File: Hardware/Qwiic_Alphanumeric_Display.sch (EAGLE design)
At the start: 16 parts, among them J1 PTH, J2 Qwiic Right Angle, U2 HT16K33

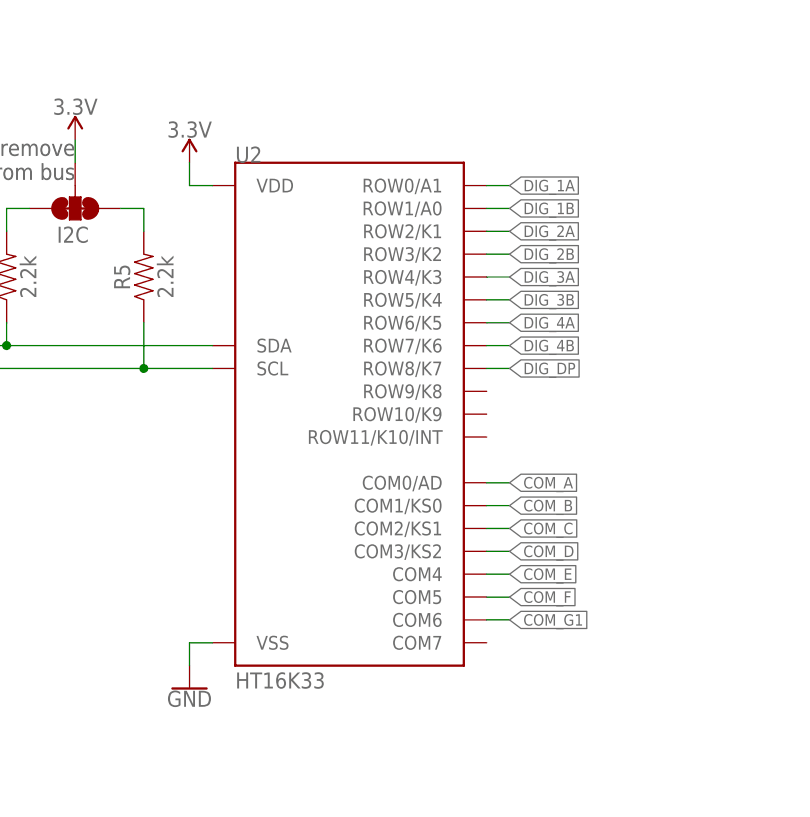
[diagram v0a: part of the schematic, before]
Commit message: New Board Layout
The pins were remapped with the LED Driver and the Display to create a better board layout.
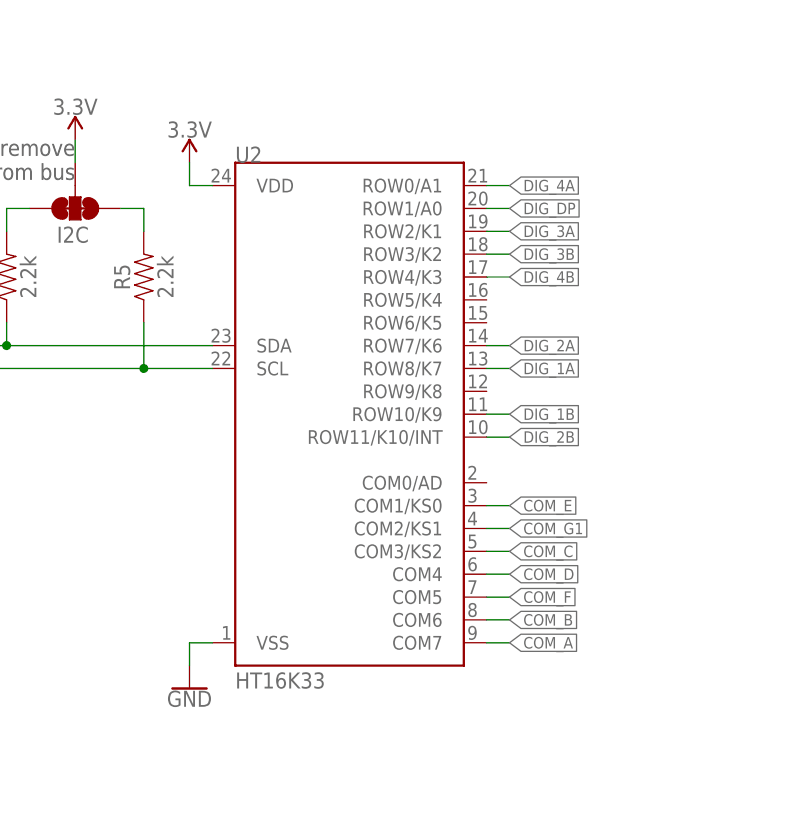
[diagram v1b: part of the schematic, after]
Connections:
- net COM_A: now also U2.COM7; no longer U2.COM0/AD
- net COM_B: now also U2.COM6; no longer U2.COM1/KS0
- net COM_C: now also U2.COM3/KS2; no longer U2.COM2/KS1
- net COM_D: now also U2.COM4; no longer U2.COM3/KS2
- net COM_E: now also U2.COM1/KS0; no longer U2.COM4
- net COM_G1: now also U2.COM2/KS1; no longer U2.COM6
- net DIG_1A: now also U2.ROW8/K7; no longer U2.ROW0/A1
- net DIG_1B: now also U2.ROW10/K9; no longer U2.ROW1/A0
- net DIG_2A: now also U2.ROW7/K6; no longer U2.ROW2/K1
- net DIG_2B: now also U2.ROW11/K10/INT; no longer U2.ROW3/K2
- net DIG_3A: now also U2.ROW2/K1; no longer U2.ROW4/K3
- net DIG_3B: now also U2.ROW3/K2; no longer U2.ROW5/K4
- net DIG_4A: now also U2.ROW0/A1; no longer U2.ROW6/K5
- net DIG_4B: now also U2.ROW4/K3; no longer U2.ROW7/K6
- net DIG_DP: now also U2.ROW1/A0; no longer U2.ROW8/K7

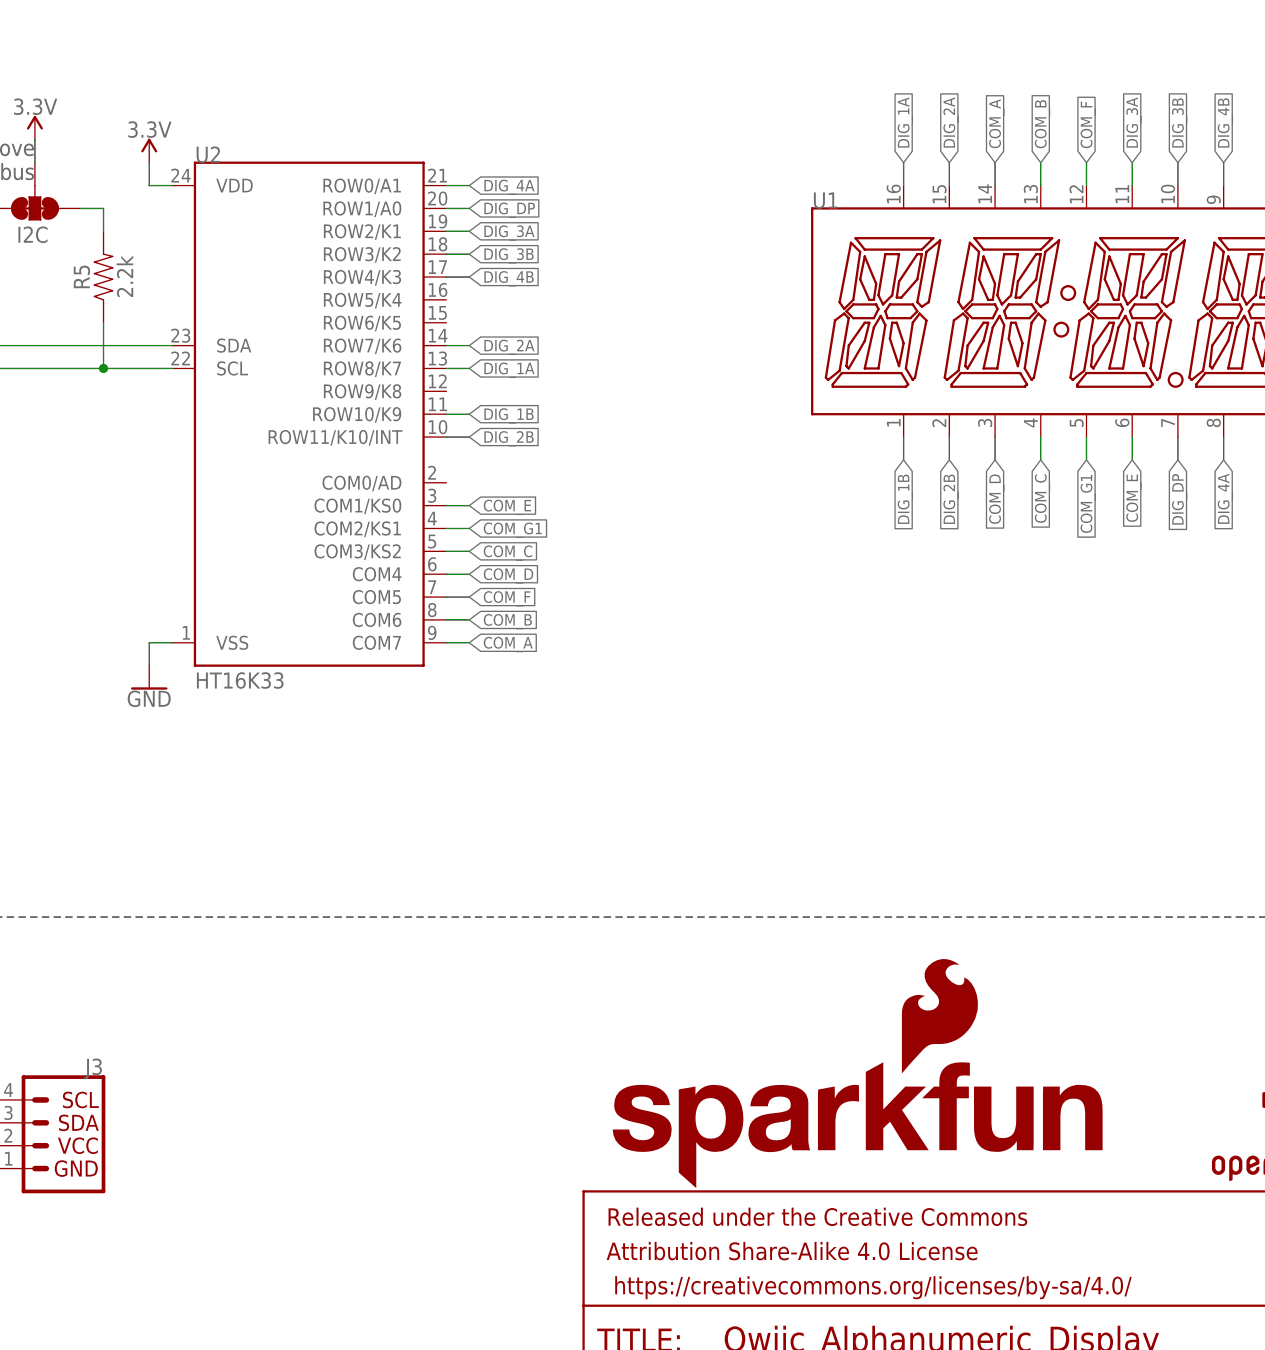
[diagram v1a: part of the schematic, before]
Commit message: Created new Board
Recreated the board in the new Branch with different pin mappings between the HT16K33 and the LED Display for easier routing
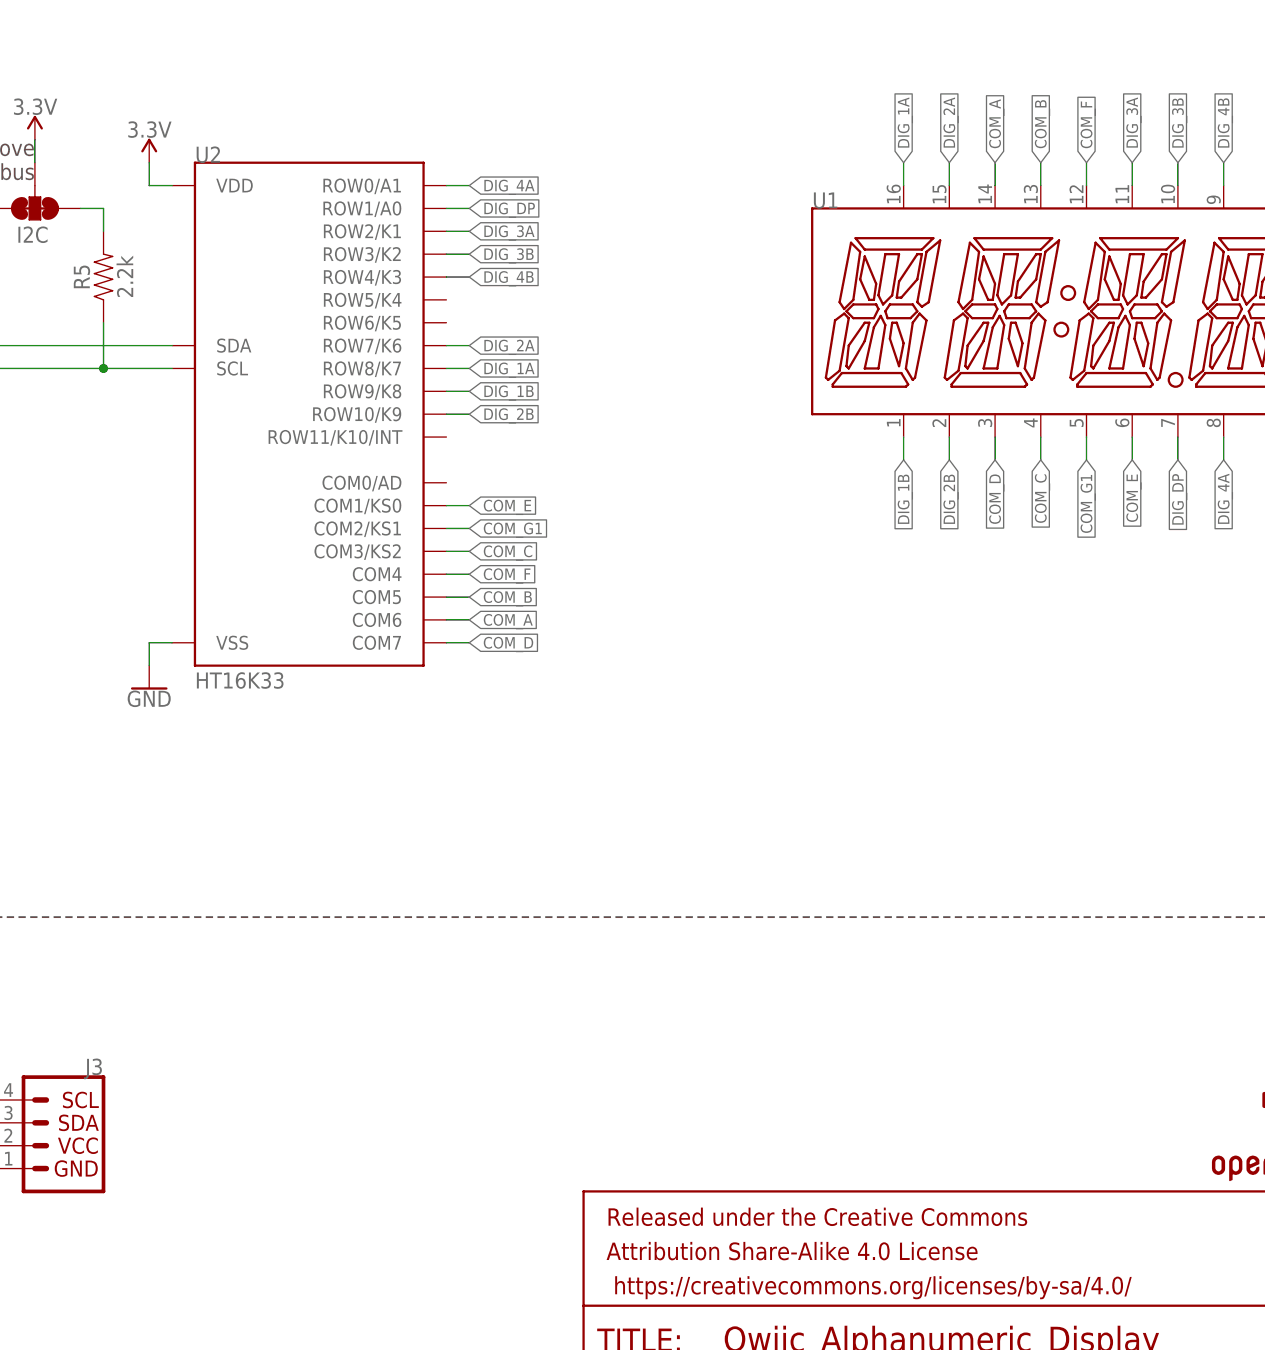
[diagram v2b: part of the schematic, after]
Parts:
- removed LOGO2: SFE_LOGO_NAME_FLAME.1_INCH, SparkFun-Aesthetics:SFE_LOGO_NAME_FLAME.1_INCH
- J3: device SparkFun-Connectors:I2C_STANDARD -> SparkFun-Connectors:I2C_STANDARD_NO_SILK
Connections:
- net COM_A: now also U2.COM6; no longer U2.COM7
- net COM_B: now also U2.COM5; no longer U2.COM6
- net COM_D: now also U2.COM7; no longer U2.COM4
- net COM_F: now also U2.COM4; no longer U2.COM5
- net DIG_1B: now also U2.ROW9/K8; no longer U2.ROW10/K9
- net DIG_2B: now also U2.ROW10/K9; no longer U2.ROW11/K10/INT
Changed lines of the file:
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@@
 <layers>
 <layer number="1" name="Top" color="4" fill="1" visible="no" active="no"/>
-<layer number="2" name="Route2" color="1" fill="3" visible="no" active="no"/>
-<layer number="15" name="Route15" color="4" fill="6" visible="no" active="no"/>
+<layer number="2" name="Route2" color="16" fill="1" visible="no" active="no"/>
+<layer number="15" name="Route15" color="23" fill="1" visible="no" active="no"/>
 <layer number="16" name="Bottom" color="1" fill="1" visible="no" active="no"/>
 <layer number="17" name="Pads" color="2" fill="1" visible="no" active="no"/>
 <layer number="18" name="Vias" color="2" fill="1" visible="no" active="no"/>
 <layer number="19" name="Unrouted" color="6" fill="1" visible="no" active="no"/>
-<layer number="20" name="Dimension" color="15" fill="1" visible="no" active="no"/>
+<layer number="20" name="Dimension" color="24" fill="1" visible="no" active="no"/>
 <layer number="21" name="tPlace" color="16" fill="1" visible="no" active="no"/>
 <layer number="22" name="bPlace" color="14" fill="1" visible="no" active="no"/>
@@
 <layer number="27" name="tValues" color="7" fill="1" visible="no" active="no"/>
 <layer number="28" name="bValues" color="7" fill="1" visible="no" active="no"/>
-<layer number="29" name="tStop" color="15" fill="3" visible="no" active="no"/>
+<layer number="29" name="tStop" color="7" fill="3" visible="no" active="no"/>
 <layer number="30" name="bStop" color="7" fill="6" visible="no" active="no"/>
 <layer number="31" name="tCream" color="7" fill="4" visible="no" active="no"/>
@@
 <layer number="47" name="Measures" color="7" fill="1" visible="no" active="no"/>
 <layer number="48" name="Document" color="7" fill="1" visible="no" active="no"/>
-<layer number="49" name="Reference" color="13" fill="1" visible="no" active="no"/>
+<layer number="49" name="Reference" color="7" fill="1" visible="no" active="no"/>
 <layer number="50" name="dxf" color="7" fill="1" visible="no" active="no"/>
 <layer number="51" name="tDocu" color="6" fill="1" visible="no" active="no"/>
@@
 <part name="J1" library="SparkFun-Connectors" deviceset="I2C_STANDARD" device="QWIIC" value="PTH"/>
 <part name="J2" library="SparkFun-Connectors" deviceset="I2C_STANDARD" device="QWIIC" value="Qwiic Right Angle"/>
-<part name="J3" library="SparkFun-Connectors" deviceset="I2C_STANDARD" device=""/>
+<part name="J3" library="SparkFun-Connectors" deviceset="I2C_STANDARD" device="_NO_SILK"/>
 <part name="SUPPLY1" library="SparkFun-PowerSymbols" deviceset="3.3V" device=""/>
 <part name="R1" library="SparkFun-Resistors" deviceset="1KOHM" device="-0603-1/10W-1%" value="1k"/>
@@
 <part name="U1" library="Alphanumeric_Display_Library" deviceset="SILSMART_DISPLAY" device=""/>
 <part name="U2" library="Alphanumeric_Display_Library" deviceset="HT16K33" device="" value="HT16K33"/>
-<part name="LOGO2" library="SparkFun-Aesthetics" deviceset="SFE_LOGO_NAME_FLAME" device=".1_INCH"/>
 </parts>
 <sheets>
@@
 <attribute name="VALUE" x="104.14" y="91.44" size="1.778" layer="96"/>
 </instance>
-<instance part="LOGO2" gate="G$1" x="149.86" y="35.56" smashed="yes"/>
 </instances>
 <busses>
@@
 </segment>
 <segment>
+<pinref part="U2" gate="G$1" pin="ROW9/K8"/>
+<wire x1="132.08" y1="124.46" x2="134.62" y2="124.46" width="0.1524" layer="91"/>
+<label x="134.62" y="124.46" size="1.27" layer="95" xref="yes"/>
+</segment>
+</net>
+<net name="DIG_2A" class="0">
+<segment>
+<wire x1="187.96" y1="147.32" x2="187.96" y2="149.86" width="0.1524" layer="91"/>
+<label x="187.96" y="149.86" size="1.27" layer="95" rot="R90" xref="yes"/>
+<pinref part="U1" gate="G$1" pin="DIG_2A"/>
+</segment>
+<segment>
+<wire x1="132.08" y1="129.54" x2="134.62" y2="129.54" width="0.1524" layer="91"/>
+<pinref part="U2" gate="G$1" pin="ROW7/K6"/>
+<label x="134.62" y="129.54" size="1.27" layer="95" xref="yes"/>
+</segment>
+</net>
+<net name="DIG_2B" class="0">
+<segment>
+<wire x1="187.96" y1="119.38" x2="187.96" y2="116.84" width="0.1524" layer="91"/>
+<label x="187.96" y="116.84" size="1.27" layer="95" rot="R270" xref="yes"/>
+<pinref part="U1" gate="G$1" pin="DIG_2B"/>
+</segment>
+<segment>
 <pinref part="U2" gate="G$1" pin="ROW10/K9"/>
 <wire x1="132.08" y1="121.92" x2="134.62" y2="121.92" width="0.1524" layer="91"/>
@@
 </segment>
 </net>
-<net name="DIG_2A" class="0">
-<segment>
-<wire x1="187.96" y1="147.32" x2="187.96" y2="149.86" width="0.1524" layer="91"/>
-<label x="187.96" y="149.86" size="1.27" layer="95" rot="R90" xref="yes"/>
-<pinref part="U1" gate="G$1" pin="DIG_2A"/>
-</segment>
-<segment>
-<wire x1="132.08" y1="129.54" x2="134.62" y2="129.54" width="0.1524" layer="91"/>
-<pinref part="U2" gate="G$1" pin="ROW7/K6"/>
-<label x="134.62" y="129.54" size="1.27" layer="95" xref="yes"/>
-</segment>
-</net>
-<net name="DIG_2B" class="0">
-<segment>
-<wire x1="187.96" y1="119.38" x2="187.96" y2="116.84" width="0.1524" layer="91"/>
-<label x="187.96" y="116.84" size="1.27" layer="95" rot="R270" xref="yes"/>
-<pinref part="U1" gate="G$1" pin="DIG_2B"/>
-</segment>
-<segment>
-<pinref part="U2" gate="G$1" pin="ROW11/K10/INT"/>
-<wire x1="132.08" y1="119.38" x2="134.62" y2="119.38" width="0.1524" layer="91"/>
-<label x="134.62" y="119.38" size="1.27" layer="95" xref="yes"/>
-</segment>
-</net>
 <net name="DIG_3A" class="0">
 <segment>
@@
 </segment>
 <segment>
+<wire x1="132.08" y1="99.06" x2="134.62" y2="99.06" width="0.1524" layer="91"/>
+<pinref part="U2" gate="G$1" pin="COM6"/>
+<label x="134.62" y="99.06" size="1.27" layer="95" xref="yes"/>
+</segment>
+</net>
+<net name="COM_B" class="0">
+<segment>
+<wire x1="198.12" y1="147.32" x2="198.12" y2="149.86" width="0.1524" layer="91"/>
+<label x="198.12" y="149.86" size="1.27" layer="95" rot="R90" xref="yes"/>
+<pinref part="U1" gate="G$1" pin="COM_B"/>
+</segment>
+<segment>
+<wire x1="132.08" y1="101.6" x2="134.62" y2="101.6" width="0.1524" layer="91"/>
+<pinref part="U2" gate="G$1" pin="COM5"/>
+<label x="134.62" y="101.6" size="1.27" layer="95" xref="yes"/>
+</segment>
+</net>
+<net name="COM_C" class="0">
+<segment>
+<wire x1="198.12" y1="119.38" x2="198.12" y2="116.84" width="0.1524" layer="91"/>
+<label x="198.12" y="116.84" size="1.27" layer="95" rot="R270" xref="yes"/>
+<pinref part="U1" gate="G$1" pin="COM_C"/>
+</segment>
+<segment>
+<wire x1="132.08" y1="106.68" x2="134.62" y2="106.68" width="0.1524" layer="91"/>
+<pinref part="U2" gate="G$1" pin="COM3/KS2"/>
+<label x="134.62" y="106.68" size="1.27" layer="95" xref="yes"/>
+</segment>
+</net>
+<net name="COM_D" class="0">
+<segment>
+<wire x1="193.04" y1="119.38" x2="193.04" y2="116.84" width="0.1524" layer="91"/>
+<label x="193.04" y="116.84" size="1.27" layer="95" rot="R270" xref="yes"/>
+<pinref part="U1" gate="G$1" pin="COM_D"/>
+</segment>
+<segment>
 <pinref part="U2" gate="G$1" pin="COM7"/>
 <wire x1="132.08" y1="96.52" x2="134.62" y2="96.52" width="0.1524" layer="91"/>
@@
 </segment>
 </net>
-<net name="COM_B" class="0">
-<segment>
-<wire x1="198.12" y1="147.32" x2="198.12" y2="149.86" width="0.1524" layer="91"/>
-<label x="198.12" y="149.86" size="1.27" layer="95" rot="R90" xref="yes"/>
-<pinref part="U1" gate="G$1" pin="COM_B"/>
-</segment>
-<segment>
-<wire x1="132.08" y1="99.06" x2="134.62" y2="99.06" width="0.1524" layer="91"/>
-<pinref part="U2" gate="G$1" pin="COM6"/>
-<label x="134.62" y="99.06" size="1.27" layer="95" xref="yes"/>
-</segment>
-</net>
-<net name="COM_C" class="0">
-<segment>
-<wire x1="198.12" y1="119.38" x2="198.12" y2="116.84" width="0.1524" layer="91"/>
-<label x="198.12" y="116.84" size="1.27" layer="95" rot="R270" xref="yes"/>
-<pinref part="U1" gate="G$1" pin="COM_C"/>
-</segment>
-<segment>
-<wire x1="132.08" y1="106.68" x2="134.62" y2="106.68" width="0.1524" layer="91"/>
-<pinref part="U2" gate="G$1" pin="COM3/KS2"/>
-<label x="134.62" y="106.68" size="1.27" layer="95" xref="yes"/>
-</segment>
-</net>
-<net name="COM_D" class="0">
-<segment>
-<wire x1="193.04" y1="119.38" x2="193.04" y2="116.84" width="0.1524" layer="91"/>
-<label x="193.04" y="116.84" size="1.27" layer="95" rot="R270" xref="yes"/>
-<pinref part="U1" gate="G$1" pin="COM_D"/>
+<net name="COM_E" class="0">
+<segment>
+<wire x1="208.28" y1="119.38" x2="208.28" y2="116.84" width="0.1524" layer="91"/>
+<label x="208.28" y="116.84" size="1.27" layer="95" rot="R270" xref="yes"/>
+<pinref part="U1" gate="G$1" pin="COM_E"/>
+</segment>
+<segment>
+<wire x1="132.08" y1="111.76" x2="134.62" y2="111.76" width="0.1524" layer="91"/>
+<pinref part="U2" gate="G$1" pin="COM1/KS0"/>
+<label x="134.62" y="111.76" size="1.27" layer="95" xref="yes"/>
+</segment>
+</net>
+<net name="COM_F" class="0">
+<segment>
+<wire x1="203.2" y1="147.32" x2="203.2" y2="149.86" width="0.1524" layer="91"/>
+<label x="203.2" y="149.86" size="1.27" layer="95" rot="R90" xref="yes"/>
+<pinref part="U1" gate="G$1" pin="COM_F"/>
 </segment>
 <segment>
@@
 </segment>
 </net>
-<net name="COM_E" class="0">
-<segment>
-<wire x1="208.28" y1="119.38" x2="208.28" y2="116.84" width="0.1524" layer="91"/>
-<label x="208.28" y="116.84" size="1.27" layer="95" rot="R270" xref="yes"/>
-<pinref part="U1" gate="G$1" pin="COM_E"/>
-</segment>
-<segment>
-<wire x1="132.08" y1="111.76" x2="134.62" y2="111.76" width="0.1524" layer="91"/>
-<pinref part="U2" gate="G$1" pin="COM1/KS0"/>
-<label x="134.62" y="111.76" size="1.27" layer="95" xref="yes"/>
-</segment>
-</net>
-<net name="COM_F" class="0">
-<segment>
-<wire x1="203.2" y1="147.32" x2="203.2" y2="149.86" width="0.1524" layer="91"/>
-<label x="203.2" y="149.86" size="1.27" layer="95" rot="R90" xref="yes"/>
-<pinref part="U1" gate="G$1" pin="COM_F"/>
-</segment>
-<segment>
-<wire x1="132.08" y1="101.6" x2="134.62" y2="101.6" width="0.1524" layer="91"/>
-<pinref part="U2" gate="G$1" pin="COM5"/>
-<label x="134.62" y="101.6" size="1.27" layer="95" xref="yes"/>
-</segment>
-</net>
